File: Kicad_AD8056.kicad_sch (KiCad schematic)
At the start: 4 parts, among them J1 Conn_Coaxial, U1 AD8056AR

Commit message: add new pcb
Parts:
- added J2: Screw_Terminal_01x03, TerminalBlock:TerminalBlock_bornier-3_P5.08mm, symbol Connector:Screw_Terminal_01x03
- added J3: Conn_Coaxial, Connector_Coaxial:BNC_Amphenol_B6252HB-NPP3G-50_Horizontal, symbol Connector:Conn_Coaxial
- added J4, J5, J6: Conn_01x01_Pin, Connector_Pin:Pin_D1.0mm_L10.0mm, symbol Connector:Conn_01x01_Pin
- added RV1: 20 KOhm, Potentiometer_THT:Potentiometer_Alps_RK163_Single_Horizontal, symbol Device:R_Potentiometer
- R1: value R -> 10 KOhm; footprint (none) -> Resistor_SMD:R_0805_2012Metric
- R2: value R -> 20 KOhm; footprint (none) -> Resistor_SMD:R_0805_2012Metric
- U1: footprint Package_SO:SOIC-8-1EP_3.9x4.9mm_P1.27mm_EP2.29x3mm -> Package_SO:SSOP-8_3.9x5.05mm_P1.27mm
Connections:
- net GND: now also J2.3 (Pin_3), J3.2 (Ext)
- net at R2.2, U1.1: now also J3.1 (In), J5.1 (Pin_1)
- net at J1.1 (In), R1.1: now also J6.1 (Pin_1)
- net at U1.3 (+): now also J4.1 (Pin_1), RV1.2
- net -5V: now reaches U1.4 (V-)
- net -5V: now also J2.2 (Pin_2), RV1.3
- net +5V: now reaches U1.8 (V+)
- net +5V: now also J2.1 (Pin_1), RV1.1
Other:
- moved on the sheet: U1B

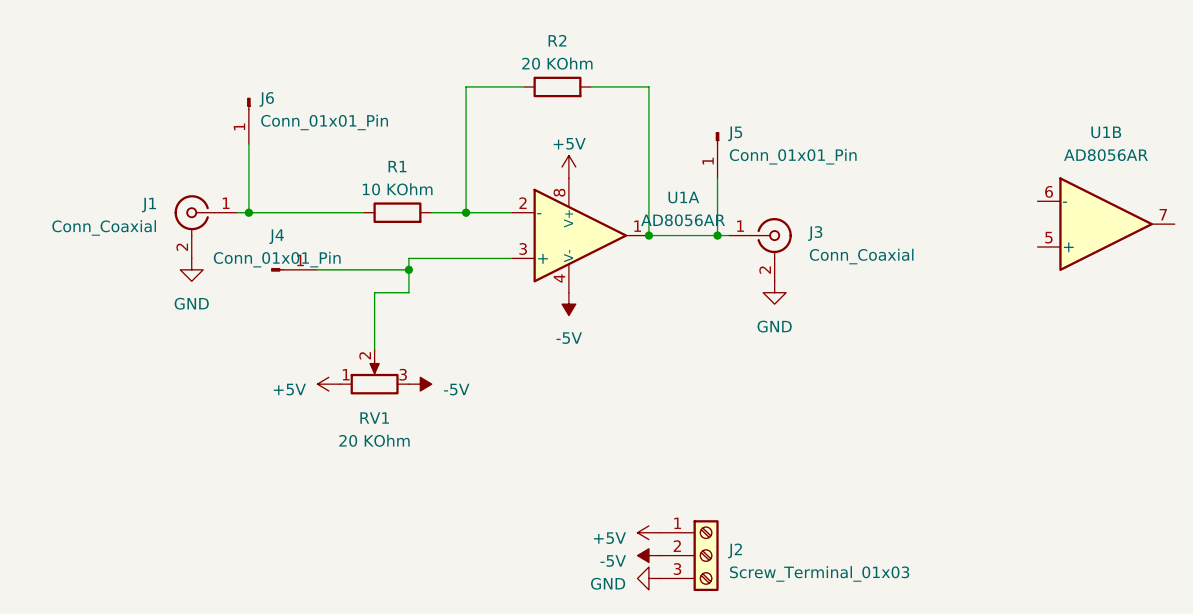
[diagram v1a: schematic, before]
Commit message: add new pcb prototype
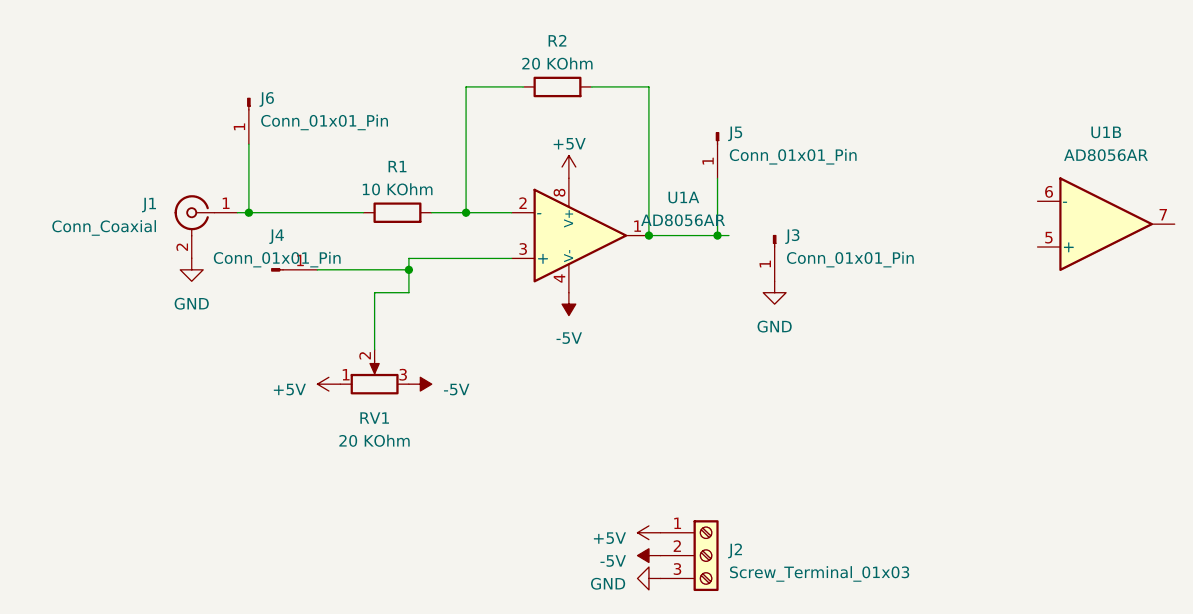
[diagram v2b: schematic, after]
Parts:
- removed J3: Conn_Coaxial, Connector_Coaxial:BNC_Amphenol_B6252HB-NPP3G-50_Horizontal, symbol Connector:Conn_Coaxial
- added J3: Conn_01x01_Pin, Connector_Pin:Pin_D1.0mm_L10.0mm, symbol Connector:Conn_01x01_Pin
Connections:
- net GND: now also J3.1 (Pin_1)
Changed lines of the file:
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@@
+    )
+  )
+  (symbol (lib_id "Connector:Conn_01x01_Pin") (at 116.84 66.04 270) (unit 1)
+    (in_bom yes) (on_board yes) (dnp no) (fields_autoplaced)
+    (property "Reference" "J3" (at 118.11 66.04 90)
+      (effects (font (size 1.27 1.27)) (justify left))
+    )
+    (property "Value" "Conn_01x01_Pin" (at 118.11 68.58 90)
+      (effects (font (size 1.27 1.27)) (justify left))
+    )
+    (property "Footprint" "Connector_Pin:Pin_D1.0mm_L10.0mm" (at 116.84 66.04 0)
+      (effects (font (size 1.27 1.27)) hide)
+    )
+    (property "Datasheet" "~" (at 116.84 66.04 0)
+      (effects (font (size 1.27 1.27)) hide)
+    )
+    (pin "1")
+    (instances
+      (project "Kicad_AD8056"
+        (path "/a1050240-6afd-4d64-aa63-d05004cefa40"
+          (reference "J3") (unit 1)
+        )
+      )
     )
   )
@@
         )
       )
-    )
-  )
-  (symbol (lib_id "Connector:Conn_Coaxial") (at 116.84 66.04 0) (unit 1)
-    (in_bom yes) (on_board yes) (dnp no) (fields_autoplaced)
-    (property "Reference" "J3" (at 120.65 65.6982 0)
-      (effects (font (size 1.27 1.27)) (justify left))
-    )
-    (property "Value" "Conn_Coaxial" (at 120.65 68.2382 0)
-      (effects (font (size 1.27 1.27)) (justify left))
-    )
-    (property "Footprint" "Connector_Coaxial:BNC_Amphenol_B6252HB-NPP3G-50_Horizontal" (at 116.84 66.04 0)
-      (effects (font (size 1.27 1.27)) hide)
-    )
-    (property "Datasheet" " ~" (at 116.84 66.04 0)
-      (effects (font (size 1.27 1.27)) hide)
-    )
-    (pin "1")
-    (pin "2")
-    (instances
-      (project "Kicad_AD8056"
-        (path "/a1050240-6afd-4d64-aa63-d05004cefa40"
-          (reference "J3") (unit 1)
-        )
-      )
